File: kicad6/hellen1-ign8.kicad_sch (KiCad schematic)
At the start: 12 parts

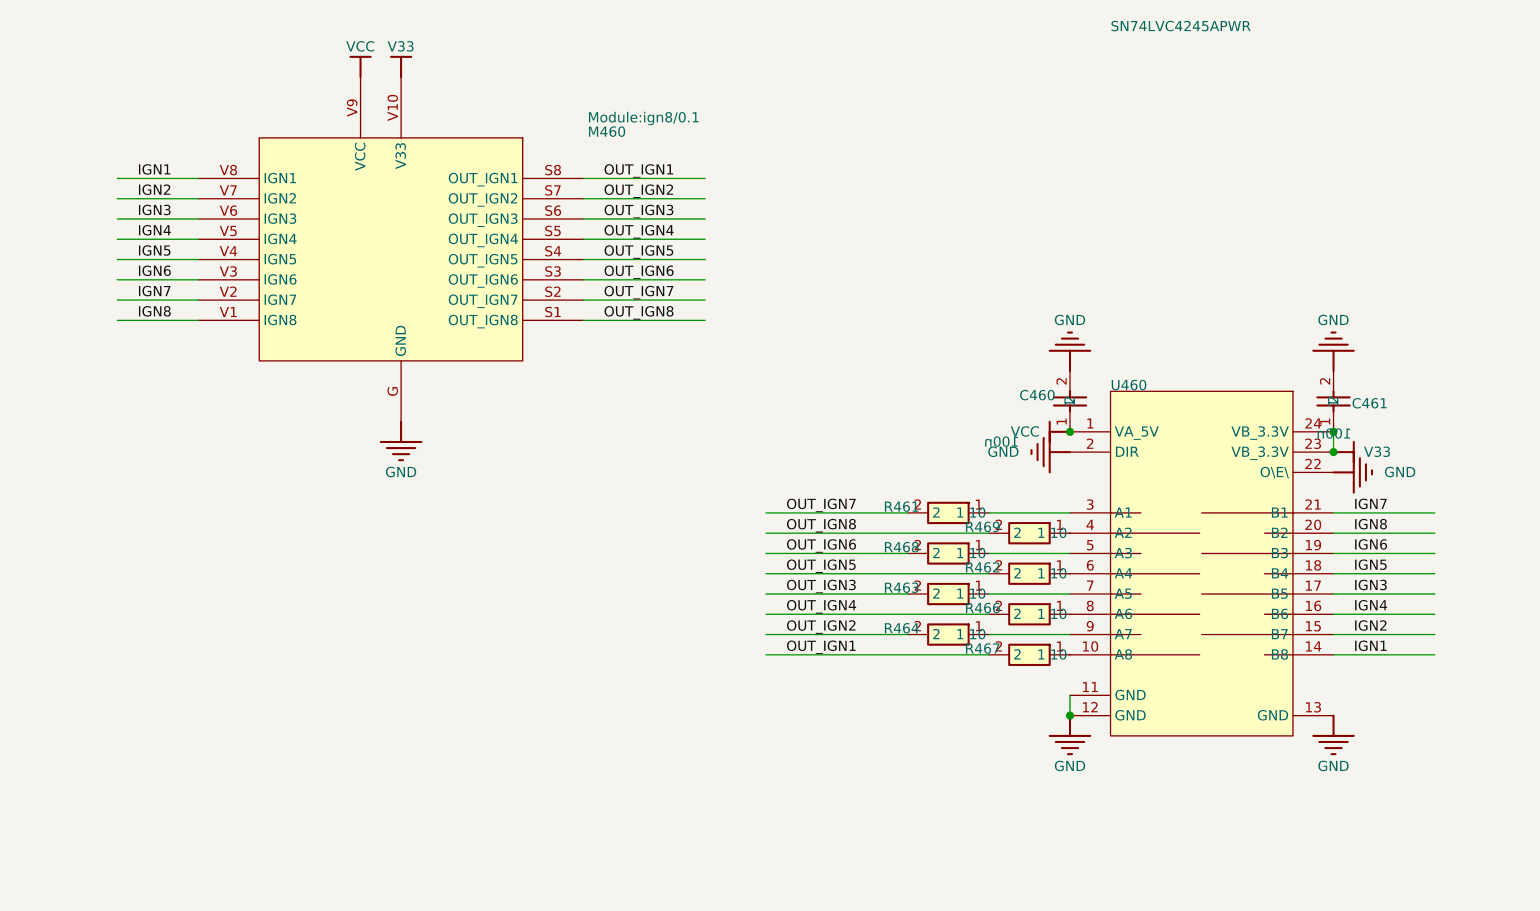
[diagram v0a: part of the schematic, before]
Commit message: move kicad src files into a separate folder
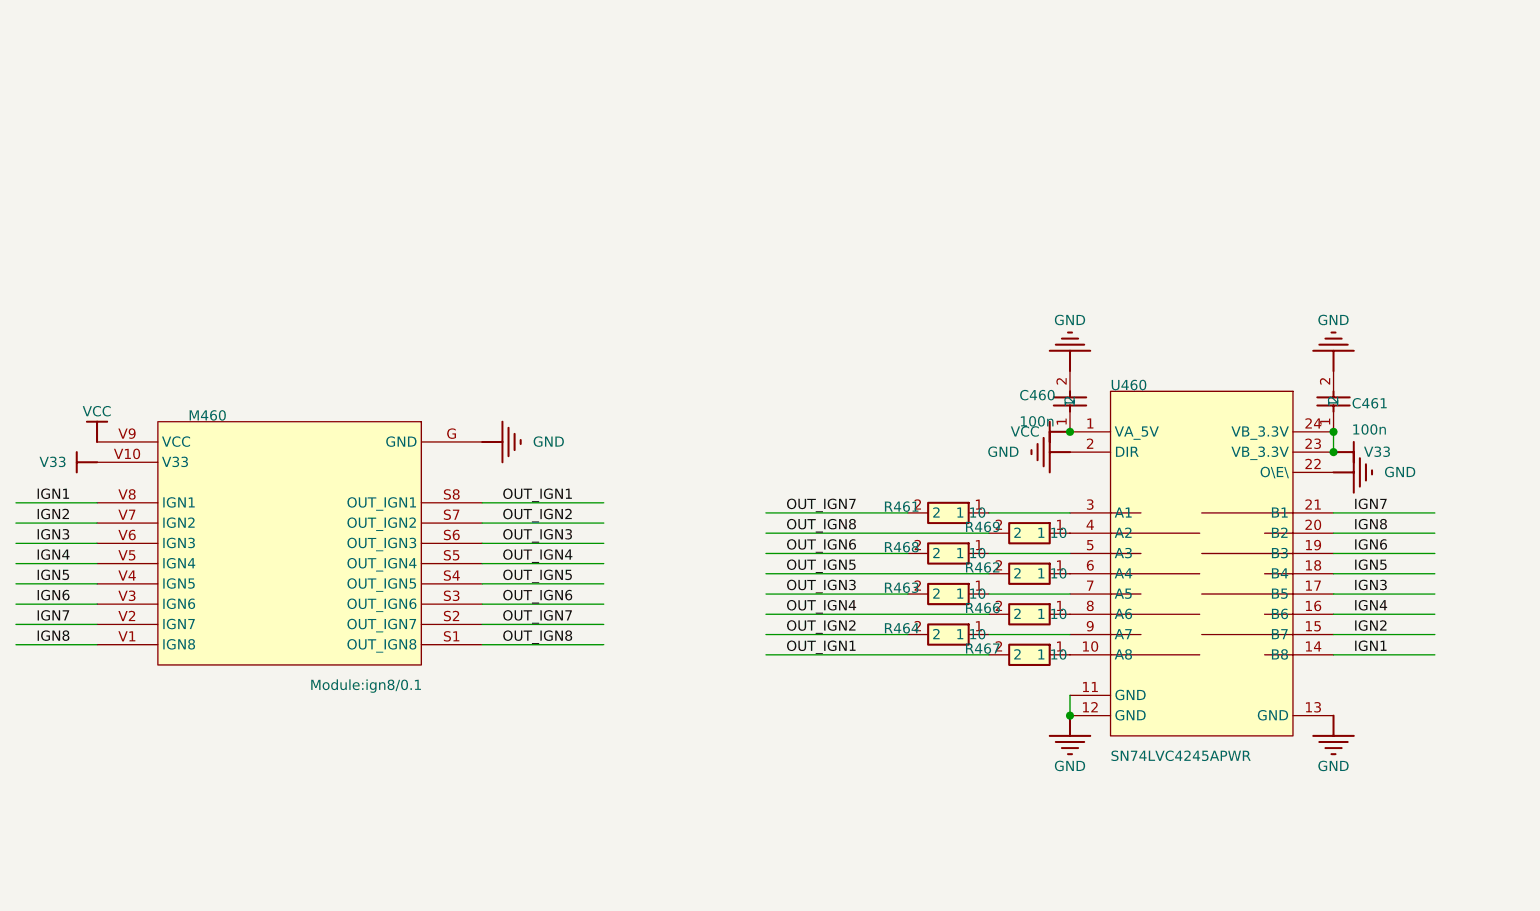
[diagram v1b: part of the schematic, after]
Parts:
- C460, C461: value (none) -> 100n; Comment 100n -> (none)
- M460: value (none) -> Module:ign8/0.1; Comment Module:ign8/0.1 -> (none)
- R461, R462, R463, R464, R466, R467, R468, R469: value (none) -> 10; Comment 10 -> (none)
- U460: value (none) -> SN74LVC4245APWR; Comment SN74LVC4245APWR -> (none)
